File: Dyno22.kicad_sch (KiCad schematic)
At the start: 41 parts, among them J1 Pwr Input, J2 Display, J3 Pwr Output, J4 BPM & Sensors, J7 UART, SW1 RotaryEncoder_Switch, U1 TS2937CW50, U2 LM324, U3 Demux

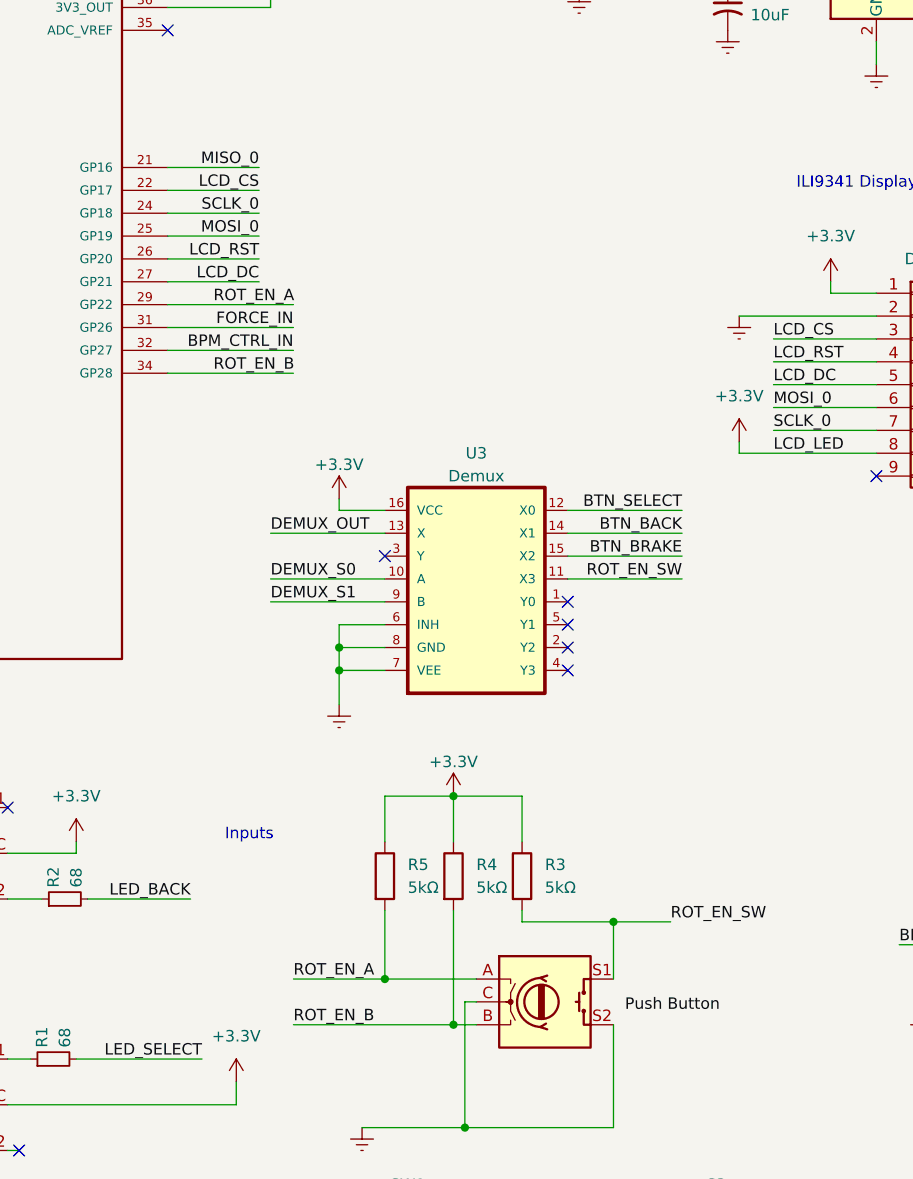
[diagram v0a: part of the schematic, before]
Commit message: Rerouted some traces for DRC and made ROT pins consecutive
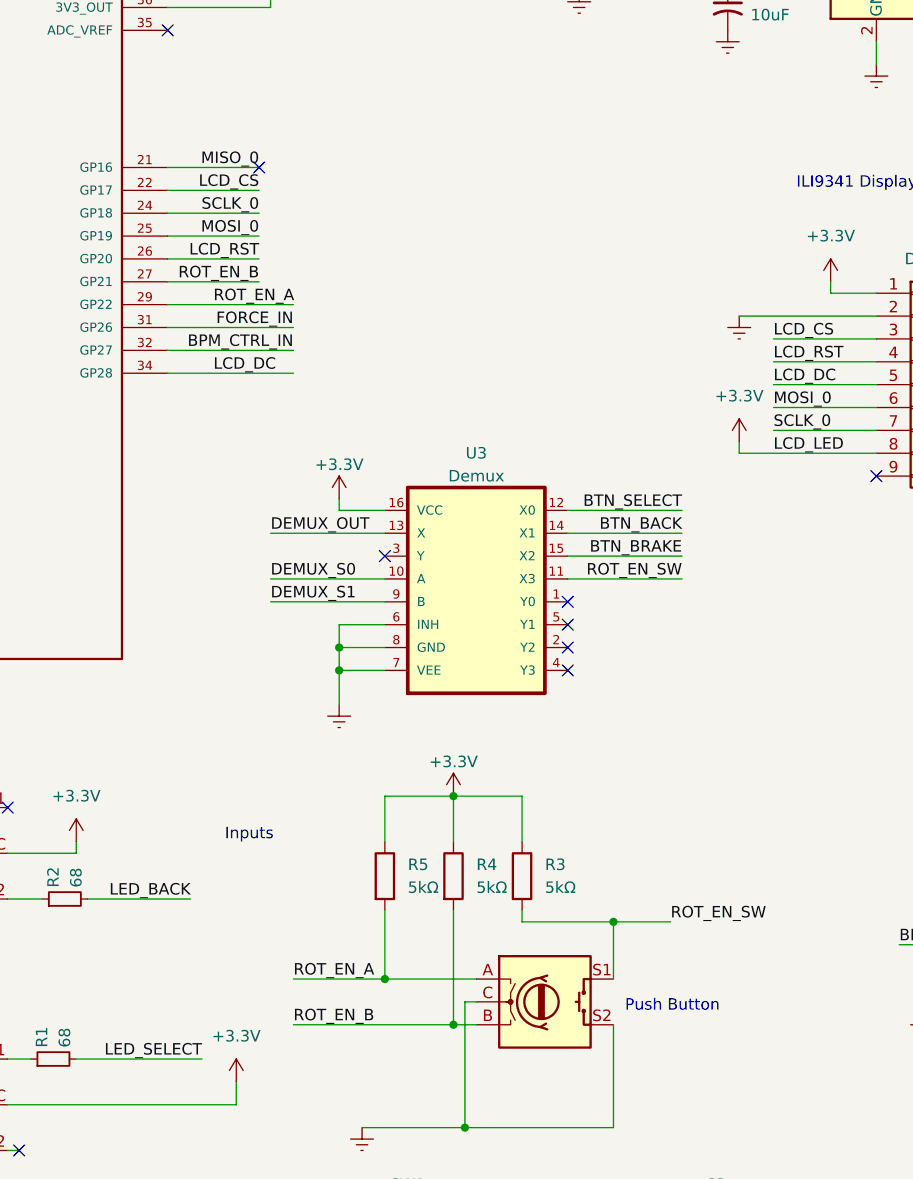
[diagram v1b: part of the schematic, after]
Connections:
- net LCD_DC: now also A1.34 (GP28); no longer A1.27 (GP21)
- net ROT_EN_B: now also A1.27 (GP21); no longer A1.34 (GP28)
- no-connect marks 14 -> 15
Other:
- note added: "Push Button"
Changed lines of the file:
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@@
   (no_connect (at 125.73 116.84))
   (no_connect (at 81.28 45.72))
+  (no_connect (at 91.44 60.96))
   (no_connect (at 64.77 170.18))
   (no_connect (at 125.73 111.76))
@@
     (effects (font (size 1.27 1.27)) (justify left bottom))
   )
+  (text "Push Button" (at 132.08 154.94 0)
+    (effects (font (size 1.27 1.27)) (justify left bottom))
+  )
   (text "Sensor / External" (at 236.22 41.91 0)
     (effects (font (size 1.27 1.27)) (justify left bottom))
@@
     (effects (font (size 1.27 1.27)) (justify left bottom))
   )
-  (label "ROT_EN_B" (at 86.36 83.82 0) (fields_autoplaced)
+  (label "LCD_DC" (at 86.36 83.82 0) (fields_autoplaced)
     (effects (font (size 1.27 1.27)) (justify left bottom))
   )
@@
     (effects (font (size 1.27 1.27)) (justify left bottom))
   )
-  (label "LCD_DC" (at 91.44 73.66 180) (fields_autoplaced)
+  (label "ROT_EN_B" (at 91.44 73.66 180) (fields_autoplaced)
     (effects (font (size 1.27 1.27)) (justify right bottom))
   )
@@
     (effects (font (size 1.27 1.27)) (justify left bottom))
   )
-  (label "Push Button" (at 132.08 154.94 0) (fields_autoplaced)
-    (effects (font (size 1.27 1.27)) (justify left bottom))
-  )

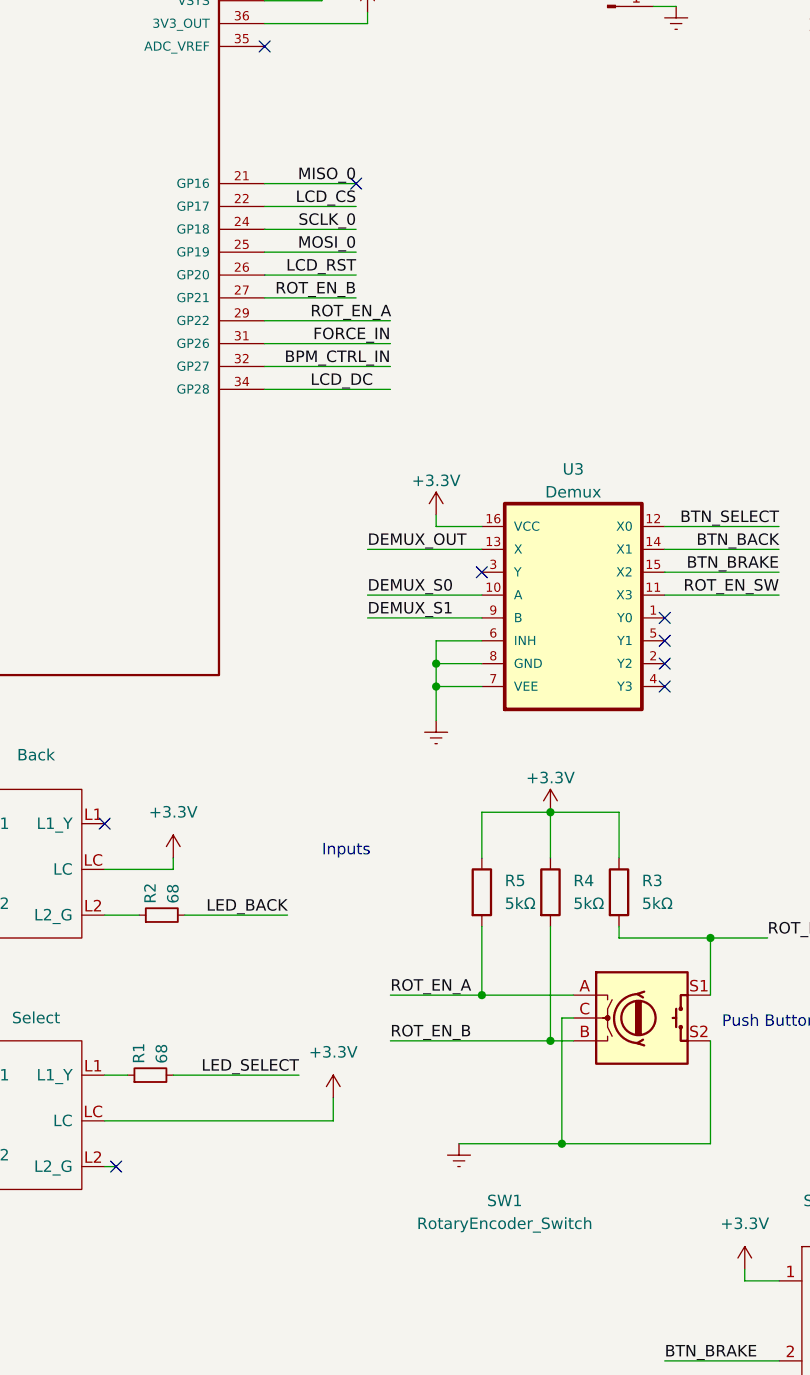
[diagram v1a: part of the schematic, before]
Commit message: Changes the rotary encoder input pins, spacing adjustments to encoder and potentiometer, increase in silkscreen text size.
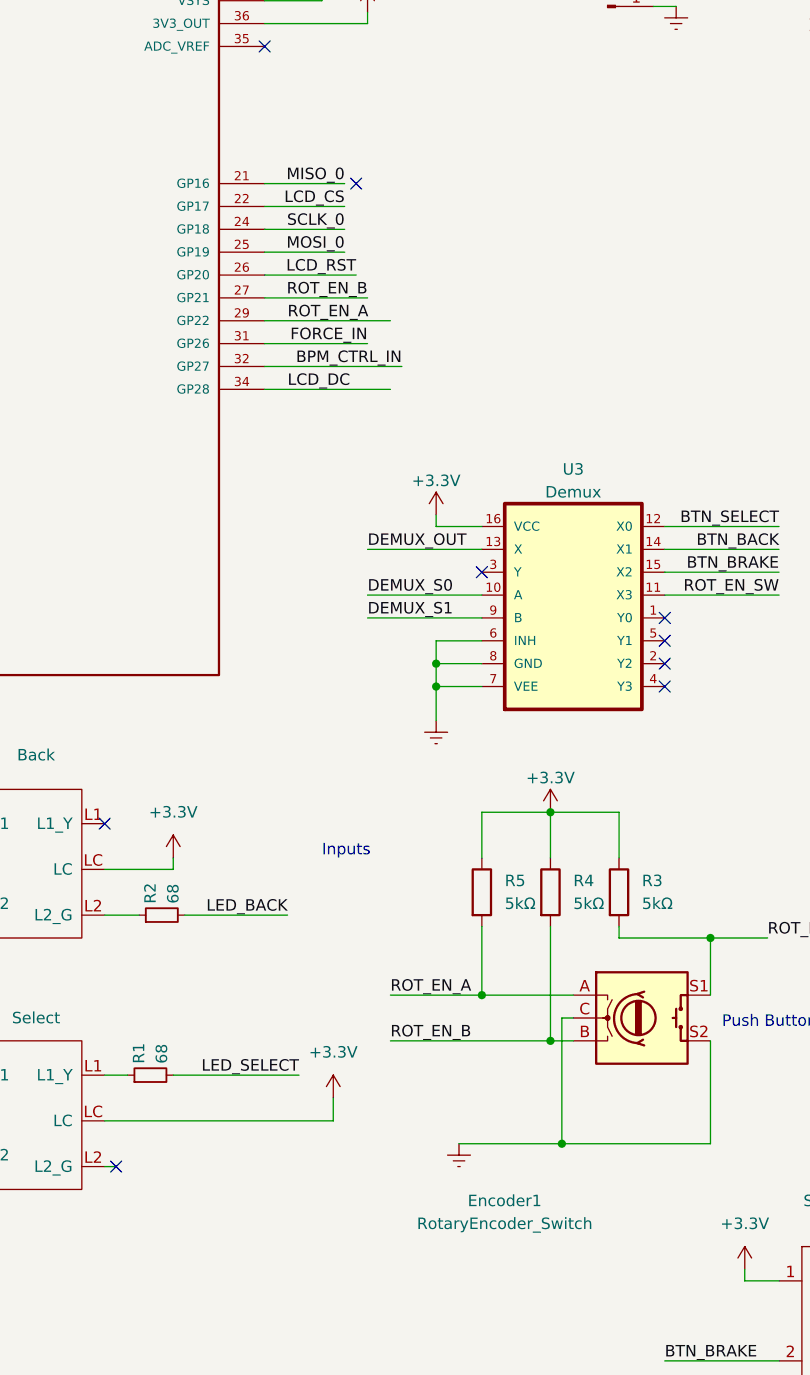
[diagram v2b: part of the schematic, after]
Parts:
- renumbered SW1 to Encoder1
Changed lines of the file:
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@@
     (stroke (width 0) (type default))
   )
-  (wire (pts (xy 81.28 73.66) (xy 91.44 73.66))
+  (wire (pts (xy 81.28 73.66) (xy 92.71 73.66))
     (stroke (width 0) (type default))
   )
@@
     (stroke (width 0) (type default))
   )
-  (wire (pts (xy 81.28 63.5) (xy 91.44 63.5))
+  (wire (pts (xy 81.28 63.5) (xy 90.17 63.5))
     (stroke (width 0) (type default))
   )
@@
     (stroke (width 0) (type default))
   )
-  (wire (pts (xy 81.28 68.58) (xy 91.44 68.58))
+  (wire (pts (xy 81.28 68.58) (xy 90.17 68.58))
     (stroke (width 0) (type default))
   )
@@
     (stroke (width 0) (type default))
   )
-  (wire (pts (xy 95.25 81.28) (xy 81.28 81.28))
+  (wire (pts (xy 96.52 81.28) (xy 81.28 81.28))
     (stroke (width 0) (type default))
   )
@@
     (stroke (width 0) (type default))
   )
-  (wire (pts (xy 81.28 60.96) (xy 91.44 60.96))
+  (wire (pts (xy 81.28 60.96) (xy 90.17 60.96))
     (stroke (width 0) (type default))
   )
@@
     (stroke (width 0) (type default))
   )
-  (wire (pts (xy 81.28 66.04) (xy 91.44 66.04))
+  (wire (pts (xy 81.28 66.04) (xy 90.17 66.04))
     (stroke (width 0) (type default))
   )
@@
     (stroke (width 0) (type default))
   )
-  (wire (pts (xy 81.28 78.74) (xy 95.25 78.74))
+  (wire (pts (xy 81.28 78.74) (xy 92.71 78.74))
     (stroke (width 0) (type default))
   )
@@
     (effects (font (size 1.27 1.27)) (justify left bottom))
   )
-  (label "LCD_CS" (at 91.44 63.5 180) (fields_autoplaced)
+  (label "LCD_CS" (at 90.17 63.5 180) (fields_autoplaced)
     (effects (font (size 1.27 1.27)) (justify right bottom))
   )
@@
     (effects (font (size 1.27 1.27)) (justify left bottom))
   )
-  (label "MISO_0" (at 91.44 60.96 180) (fields_autoplaced)
+  (label "MISO_0" (at 90.17 60.96 180) (fields_autoplaced)
     (effects (font (size 1.27 1.27)) (justify right bottom))
   )
@@
     (effects (font (size 1.27 1.27)) (justify left bottom))
   )
-  (label "LCD_DC" (at 86.36 83.82 0) (fields_autoplaced)
+  (label "LCD_DC" (at 83.82 83.82 0) (fields_autoplaced)
     (effects (font (size 1.27 1.27)) (justify left bottom))
   )
@@
     (effects (font (size 1.27 1.27)) (justify left bottom))
   )
-  (label "ROT_EN_B" (at 91.44 73.66 180) (fields_autoplaced)
+  (label "ROT_EN_B" (at 92.71 73.66 180) (fields_autoplaced)
     (effects (font (size 1.27 1.27)) (justify right bottom))
   )
-  (label "ROT_EN_A" (at 86.36 76.2 0) (fields_autoplaced)
+  (label "ROT_EN_A" (at 83.82 76.2 0) (fields_autoplaced)
     (effects (font (size 1.27 1.27)) (justify left bottom))
   )
@@
     (effects (font (size 1.27 1.27)) (justify left bottom))
   )
-  (label "SCLK_0" (at 91.44 66.04 180) (fields_autoplaced)
+  (label "SCLK_0" (at 90.17 66.04 180) (fields_autoplaced)
     (effects (font (size 1.27 1.27)) (justify right bottom))
   )
@@
     (effects (font (size 1.27 1.27)) (justify right bottom))
   )
-  (label "FORCE_IN" (at 95.25 78.74 180) (fields_autoplaced)
+  (label "FORCE_IN" (at 92.71 78.74 180) (fields_autoplaced)
     (effects (font (size 1.27 1.27)) (justify right bottom))
   )
@@
     (effects (font (size 1.27 1.27)) (justify left bottom))
   )
-  (label "BPM_CTRL_IN" (at 95.25 81.28 180) (fields_autoplaced)
+  (label "BPM_CTRL_IN" (at 96.52 81.28 180) (fields_autoplaced)
     (effects (font (size 1.27 1.27)) (justify right bottom))
   )
@@
     (effects (font (size 1.27 1.27)) (justify right bottom))
   )
-  (label "MOSI_0" (at 91.44 68.58 180) (fields_autoplaced)
+  (label "MOSI_0" (at 90.17 68.58 180) (fields_autoplaced)
     (effects (font (size 1.27 1.27)) (justify right bottom))
   )
@@
   (symbol (lib_id "Device:RotaryEncoder_Switch") (at 123.19 153.67 0) (unit 1)
     (in_bom yes) (on_board yes) (dnp no)
-    (property "Reference" "SW1" (at 107.95 173.99 0)
+    (property "Reference" "Encoder1" (at 107.95 173.99 0)
       (effects (font (size 1.27 1.27)))
     )
@@
       (project "Dyno22"
         (path "/7271225a-6695-4332-8687-d26f1f45d708"
-          (reference "SW1") (unit 1)
-        )
-      )
+          (reference "Encoder1") (unit 1)
+        )
+      )

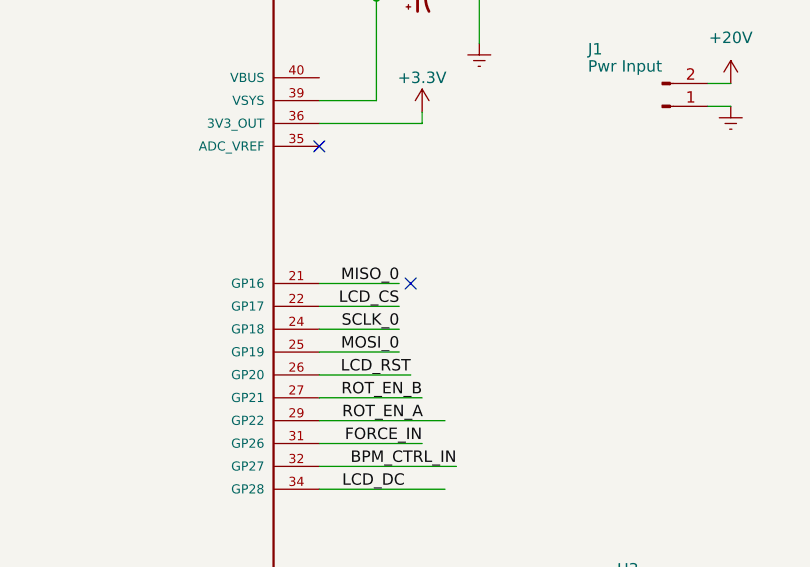
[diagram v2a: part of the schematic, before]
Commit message: Fixed traces DRC
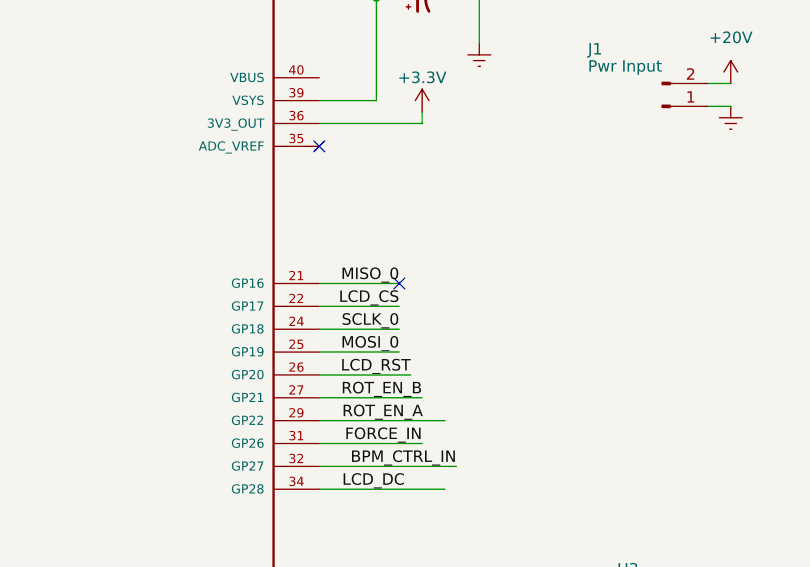
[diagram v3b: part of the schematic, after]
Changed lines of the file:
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@@
   (no_connect (at 125.73 116.84))
   (no_connect (at 81.28 45.72))
-  (no_connect (at 91.44 60.96))
+  (no_connect (at 90.17 60.96))
   (no_connect (at 64.77 170.18))
   (no_connect (at 125.73 111.76))

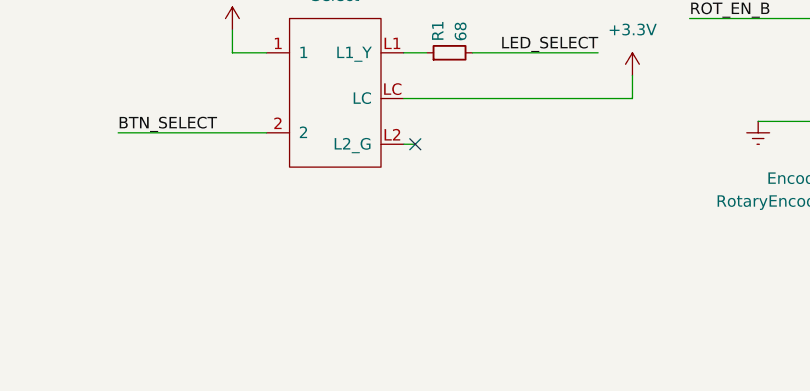
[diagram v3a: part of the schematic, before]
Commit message: moving traces for the pot
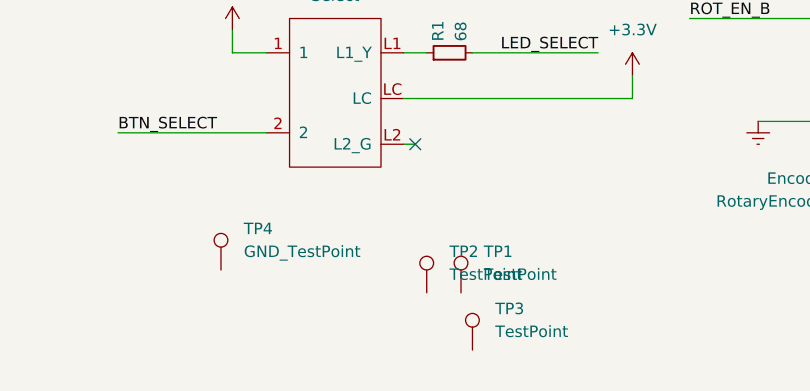
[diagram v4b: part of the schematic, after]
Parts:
- added TP1, TP2, TP3: TestPoint, symbol Connector:TestPoint
- added TP4: GND_TestPoint, TestPoint:TestPoint_Pad_4.0x4.0mm, symbol Connector:TestPoint
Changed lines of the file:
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@@
+    )
+  )
+  (symbol (lib_id "Connector:TestPoint") (at 69.85 186.69 0) (unit 1)
+    (in_bom yes) (on_board yes) (dnp no) (fields_autoplaced)
+    (property "Reference" "TP1" (at 72.39 182.118 0)
+      (effects (font (size 1.27 1.27)) (justify left))
+    )
+    (property "Value" "TestPoint" (at 72.39 184.658 0)
+      (effects (font (size 1.27 1.27)) (justify left))
+    )
+    (property "Footprint" "" (at 74.93 186.69 0)
+      (effects (font (size 1.27 1.27)) hide)
+    )
+    (property "Datasheet" "~" (at 74.93 186.69 0)
+      (effects (font (size 1.27 1.27)) hide)
+    )
+    (pin "1")
+    (instances
+      (project "Dyno22"
+        (path "/7271225a-6695-4332-8687-d26f1f45d708"
+          (reference "TP1") (unit 1)
+        )
+      )
     )
   )
@@
     )
   )
+  (symbol (lib_id "Connector:TestPoint") (at 66.04 186.69 0) (unit 1)
+    (in_bom yes) (on_board yes) (dnp no) (fields_autoplaced)
+    (property "Reference" "TP2" (at 68.58 182.118 0)
+      (effects (font (size 1.27 1.27)) (justify left))
+    )
+    (property "Value" "TestPoint" (at 68.58 184.658 0)
+      (effects (font (size 1.27 1.27)) (justify left))
+    )
+    (property "Footprint" "" (at 71.12 186.69 0)
+      (effects (font (size 1.27 1.27)) hide)
+    )
+    (property "Datasheet" "~" (at 71.12 186.69 0)
+      (effects (font (size 1.27 1.27)) hide)
+    )
+    (pin "1")
+    (instances
+      (project "Dyno22"
+        (path "/7271225a-6695-4332-8687-d26f1f45d708"
+          (reference "TP2") (unit 1)
+        )
+      )
+    )
+  )
   (symbol (lib_name "+3.3V_2") (lib_id "power:+3.3V") (at 151.765 19.685 0) (unit 1)
     (in_bom yes) (on_board yes) (dnp no) (fields_autoplaced)
@@
         (path "/7271225a-6695-4332-8687-d26f1f45d708"
           (reference "#PWR023") (unit 1)
+        )
+      )
+    )
+  )
+  (symbol (lib_id "Connector:TestPoint") (at 71.12 193.04 0) (unit 1)
+    (in_bom yes) (on_board yes) (dnp no) (fields_autoplaced)
+    (property "Reference" "TP3" (at 73.66 188.468 0)
+      (effects (font (size 1.27 1.27)) (justify left))
+    )
+    (property "Value" "TestPoint" (at 73.66 191.008 0)
+      (effects (font (size 1.27 1.27)) (justify left))
+    )
+    (property "Footprint" "" (at 76.2 193.04 0)
+      (effects (font (size 1.27 1.27)) hide)
+    )
+    (property "Datasheet" "~" (at 76.2 193.04 0)
+      (effects (font (size 1.27 1.27)) hide)
+    )
+    (pin "1")
+    (instances
+      (project "Dyno22"
+        (path "/7271225a-6695-4332-8687-d26f1f45d708"
+          (reference "TP3") (unit 1)
         )
       )
@@
         )
       )
+    )
+  )
+  (symbol (lib_id "Connector:TestPoint") (at 43.18 184.15 0) (unit 1)
+    (in_bom yes) (on_board yes) (dnp no) (fields_autoplaced)
+    (property "Reference" "TP4" (at 45.72 179.578 0)
+      (effects (font (size 1.27 1.27)) (justify left))
+    )
+    (property "Value" "GND_TestPoint" (at 45.72 182.118 0)
+      (effects (font (size 1.27 1.27)) (justify left))
+    )
+    (property "Footprint" "TestPoint:TestPoint_Pad_4.0x4.0mm" (at 48.26 184.15 0)
+      (effects (font (size 1.27 1.27)) hide)
+    )
+    (property "Datasheet" "~" (at 48.26 184.15 0)
+      (effects (font (size 1.27 1.27)) hide)
+    )
+    (pin "1")
+    (instances
+      (project "Dyno22"
+        (path "/7271225a-6695-4332-8687-d26f1f45d708"
+          (reference "TP4") (unit 1)
+        )
+      )
